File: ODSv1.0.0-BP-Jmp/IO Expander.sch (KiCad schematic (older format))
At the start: 15 parts, among them J20 Conn_02x10_Odd_Even, J21 Conn_02x10_Odd_Even, J22 Conn_02x10_Odd_Even, U3 MAX7317, U4 DACx0508xRTE, U5 AD7689xCP

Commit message: Fix incorrect pin type in the AD7689xCP symbol from KiCad
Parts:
- U5: symbol Analog_ADC:AD7689xCP -> Octopi:AD7689xCP
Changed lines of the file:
@@
 $EndComp
 $Comp
-L Analog_ADC:AD7689xCP U5
+L Octopi:AD7689xCP U5
 U 1 1 602154C4
 P 8000 3500

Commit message: Define a no-IC variant of BP-Jmp
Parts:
- U3, U4, U5: Config -NoExpansion -> -NoExpansion, -NoIC
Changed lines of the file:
@@
 F 7 "SMD" H 2500 1750 50  0001 C CNN "Type"
 F 8 "MAX7317AEE+TCT-ND" H 2500 1750 50  0001 C CNN "Digikey ID"
-F 9 "-NoExpansion" H 2500 1750 50  0001 C CNN "Config"
+F 9 "-NoExpansion, -NoIC" H 2500 1750 50  0001 C CNN "Config"
 	1    2500 1750
 	1    0    0    -1
@@
 F 2 "Package_DFN_QFN:WQFN-16-1EP_3x3mm_P0.5mm_EP1.6x1.6mm_ThermalVias" H 2500 3000 50  0001 C CNN
 F 3 "https://www.ti.com/lit/ds/symlink/dac60508.pdf" H 2500 3550 50  0001 C CNN
-F 4 "-NoExpansion" H 2500 3500 50  0001 C CNN "Config"
+F 4 "-NoExpansion, -NoIC" H 2500 3500 50  0001 C CNN "Config"
 F 5 "296-51047-1-ND" H 2500 3500 50  0001 C CNN "Digikey ID"
 F 6 "DAC80508ZRTER" H 2500 3500 50  0001 C CNN "MPN"
@@
 F 2 "Package_CSP:LFCSP-20-1EP_4x4mm_P0.5mm_EP2.5x2.5mm" H 8000 3500 50  0001 C CNN
 F 3 "https://www.analog.com/media/en/technical-documentation/data-sheets/AD7682_7689.pdf" H 8000 3500 50  0001 C CNN
-F 4 "-NoExpansion" H 8000 3500 50  0001 C CNN "Config"
+F 4 "-NoExpansion, -NoIC" H 8000 3500 50  0001 C CNN "Config"
 F 5 "AD7689BCPZRL7CT-ND" H 8000 3500 50  0001 C CNN "Digikey ID"
 F 6 "AD7689BCPZRL7" H 8000 3500 50  0001 C CNN "MPN"

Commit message: Fix problems with BP-Jmp variant configurations
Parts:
- C10, C11, C3, C4, C5, C6, C7, C8, C9: Config (none) -> -NoExpansion, -NoIC
- J20, J21, J22: Config -NoExpansion -> -NoExpansion, -NoIC
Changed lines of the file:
@@
 F 7 "SMD" H 750 1150 50  0001 C CNN "Type"
 F 8 "478-1235-1-ND" H 750 1150 50  0001 C CNN "Digikey ID"
+F 9 "-NoExpansion, -NoIC" H 750 1150 50  0001 C CNN "Config"
 	1    750  1150
 	1    0    0    -1
@@
 F 2 "Connector_PinHeader_2.54mm:PinHeader_2x10_P2.54mm_Vertical_SMD" H 3950 1700 50  0001 C CNN
 F 3 "http://suddendocs.samtec.com/catalog_english/tsm.pdf" H 3950 1700 50  0001 C CNN
-F 4 "-NoExpansion" H 3950 1700 50  0001 C CNN "Config"
+F 4 "-NoExpansion, -NoIC" H 3950 1700 50  0001 C CNN "Config"
 F 5 "SAM8990-ND" H 3950 1700 50  0001 C CNN "Digikey ID"
 F 6 "TSM-110-01-T-DV" H 3950 1700 50  0001 C CNN "MPN"
@@
 F 2 "Connector_PinHeader_2.54mm:PinHeader_2x10_P2.54mm_Vertical_SMD" H 4050 3400 50  0001 C CNN
 F 3 "http://suddendocs.samtec.com/catalog_english/tsm.pdf" H 4050 3400 50  0001 C CNN
-F 4 "-NoExpansion" H 4050 3400 50  0001 C CNN "Config"
+F 4 "-NoExpansion, -NoIC" H 4050 3400 50  0001 C CNN "Config"
 F 5 "SAM8990-ND" H 4050 3400 50  0001 C CNN "Digikey ID"
 F 6 "TSM-110-01-T-DV" H 4050 3400 50  0001 C CNN "MPN"
@@
 F 7 "SMD" H 750 3050 50  0001 C CNN "Type"
 F 8 "478-7018-1-ND" H 750 3050 50  0001 C CNN "Digikey ID"
+F 9 "-NoExpansion, -NoIC" H 750 3050 50  0001 C CNN "Config"
 	1    750  3050
 	1    0    0    -1
@@
 F 7 "SMD" H 750 3900 50  0001 C CNN "Type"
 F 8 "478-7018-1-ND" H 750 3900 50  0001 C CNN "Digikey ID"
+F 9 "-NoExpansion, -NoIC" H 750 3900 50  0001 C CNN "Config"
 	1    750  3900
 	1    0    0    -1
@@
 F 7 "SMD" H 1200 3050 50  0001 C CNN "Type"
 F 8 "478-10578-1-ND" H 1200 3050 50  0001 C CNN "Digikey ID"
+F 9 "-NoExpansion, -NoIC" H 1200 3050 50  0001 C CNN "Config"
 	1    1200 3050
 	1    0    0    -1
@@
 F 7 "SMD" H 1200 3900 50  0001 C CNN "Type"
 F 8 "478-7018-1-ND" H 1200 3900 50  0001 C CNN "Digikey ID"
+F 9 "-NoExpansion, -NoIC" H 1200 3900 50  0001 C CNN "Config"
 	1    1200 3900
 	1    0    0    -1
@@
 F 7 "SMD" H 6000 3150 50  0001 C CNN "Type"
 F 8 "478-7018-1-ND" H 6000 3150 50  0001 C CNN "Digikey ID"
+F 9 "-NoExpansion, -NoIC" H 6000 3150 50  0001 C CNN "Config"
 	1    6000 3150
 	-1   0    0    -1
@@
 F 2 "Connector_PinHeader_2.54mm:PinHeader_2x10_P2.54mm_Vertical_SMD" H 9300 3400 50  0001 C CNN
 F 3 "http://suddendocs.samtec.com/catalog_english/tsm.pdf" H 9300 3400 50  0001 C CNN
-F 4 "-NoExpansion" H 9300 3400 50  0001 C CNN "Config"
+F 4 "-NoExpansion, -NoIC" H 9300 3400 50  0001 C CNN "Config"
 F 5 "SAM8990-ND" H 9300 3400 50  0001 C CNN "Digikey ID"
 F 6 "TSM-110-01-T-DV" H 9300 3400 50  0001 C CNN "MPN"
@@
 F 7 "SMD" H 6500 3950 50  0001 C CNN "Type"
 F 8 "478-10578-1-ND" H 6500 3950 50  0001 C CNN "Digikey ID"
+F 9 "-NoExpansion, -NoIC" H 6500 3950 50  0001 C CNN "Config"
 	1    6500 3950
 	-1   0    0    -1
@@
 F 7 "SMD" H 6500 3150 50  0001 C CNN "Type"
 F 8 "478-7018-1-ND" H 6500 3150 50  0001 C CNN "Digikey ID"
+F 9 "-NoExpansion, -NoIC" H 6500 3150 50  0001 C CNN "Config"
 	1    6500 3150
 	-1   0    0    -1
@@
 F 7 "SMD" H 6000 3950 50  0001 C CNN "Type"
 F 8 "478-7018-1-ND" H 6000 3950 50  0001 C CNN "Digikey ID"
+F 9 "-NoExpansion, -NoIC" H 6000 3950 50  0001 C CNN "Config"
 	1    6000 3950
 	-1   0    0    -1

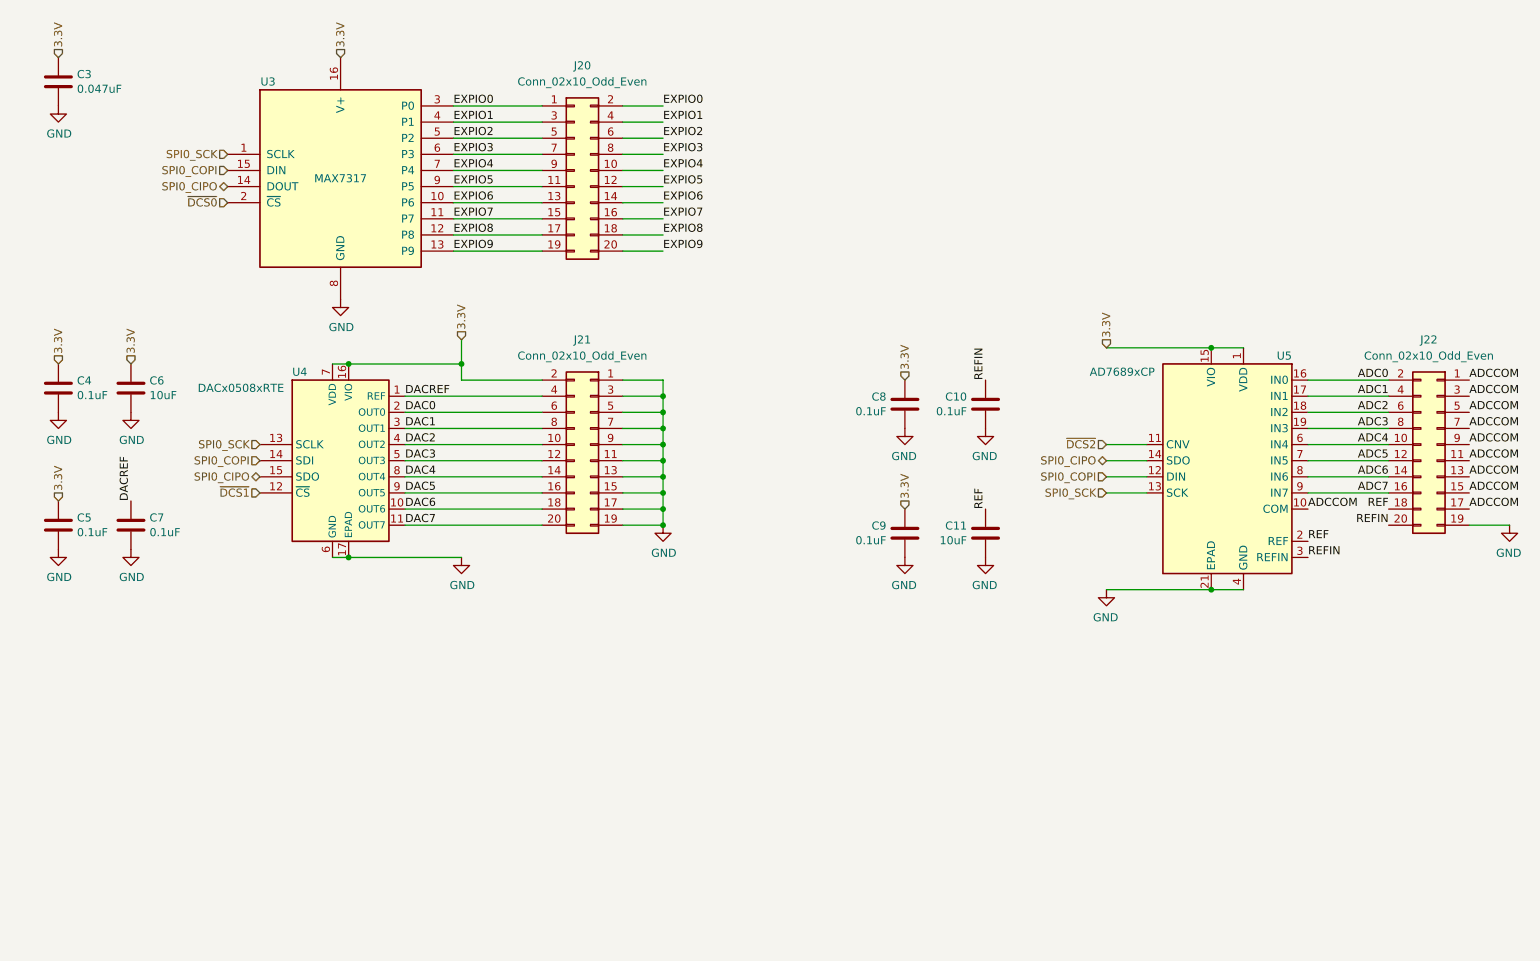
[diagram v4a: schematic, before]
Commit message: Fix implementation of SPI CS multiplexing system (#22)
* Disconnect PP-T41's MAX7317's DOUT, since it's not needed anyways (#16)

* Disconnect BT & BP-Jmp backbone MAX7317 DOUT (#16); make DOUT output pin

* Replace DAC with a second MAX7317 expander with pullup resistors

* Insert 3-state buffers between MAX7317 DOUTs and CIPO in BP-Jmp (#16)

* Update symbol fields for I/O expansion components in BP-Jmp

* Consolidate free space by moving the AD7689 chip

* Add pull-ups on demuxed DCS (#17), move pull-ups to bottom of BP-Jmp

* Insert 3-state buffers between all MAX7317 DOUTs and CIPO (#16)

* Add bypass caps to the 3-state buffers for BP-Jmp's I/O expanders

* Fix title block for SPI DCS Selector sheet in BP-Jmp

* Use 2k pullups instead of 20k pullups on BP-Jmp

* Add 2k pullups on demuxed DSCS pins in PP-T41

* Define a NoPufferfish BOM variant of PP-T41

* Adjust the 12V copper fills on PP-T41

* Add 2k pullups within the DSCS selector in PP-T41 (#17)

* Add more information to READMEs

* Add 2k pullups within DCS selectors (#17), bump BP-Jmp to 0.2.0

* Fix errors in PR template for modified boards

* Move usage on I/O peripherals into a subsection in BP-Jmp's README.md

* Update KiCad preview & mechanical renders of all boards

* Improve & consolidate pull request templates

* Update raytrace renders of the entire stack

* Add missing definition for NoPufferfish variant for PP-T41

* Add link to CADLab project for this repo

* Remove the message annoyingly added by CADLab to top of README.md
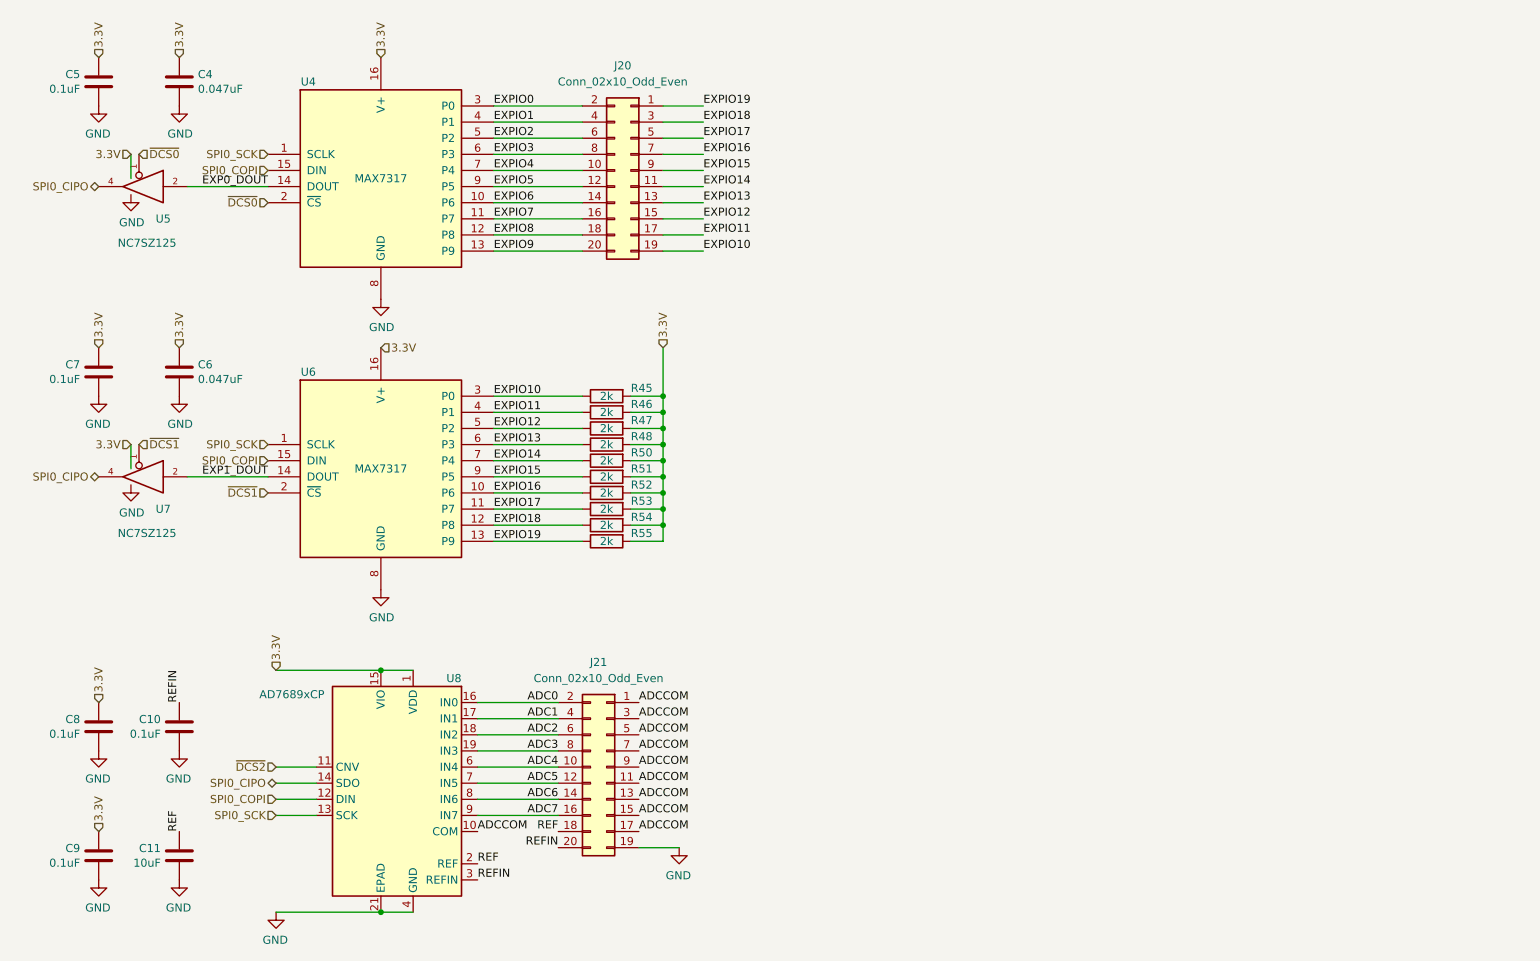
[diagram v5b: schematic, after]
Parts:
- removed C3: 0.047uF, Capacitor_SMD:C_0603_1608Metric, symbol Device:C
- removed J21: Conn_02x10_Odd_Even, Connector_PinHeader_2.54mm:PinHeader_2x10_P2.54mm_Vertical_SMD, symbol Connector_Generic:Conn_02x10_Odd_Even
- removed U4: DACx0508xRTE, Package_DFN_QFN:WQFN-16-1EP_3x3mm_P0.5mm_EP1.6x1.6mm_ThermalVias, symbol Octopi:DACx0508xRTE
- added R45, R46, R47, R48, R50, R51, R52, R53, R54, R55: 2k, Resistor_SMD:R_0603_1608Metric, symbol Device:R
- added U5, U7: NC7SZ125, Package_TO_SOT_SMD:SOT-353_SC-70-5, symbol Octopi:NC7SZ125
- added U6: MAX7317, Package_SO:QSOP-16_3.9x4.9mm_P0.635mm, symbol Octopi:MAX7317
- C4: value 0.1uF -> 0.047uF; Digikey ID 478-7018-1-ND -> 478-1235-1-ND; MPN 06033C104KAT4A -> 06033C473KAT2A; Ordering URL https://www.digikey.com/en/products/detail/avx-corporation/06033C104KAT4A/3247517 -> https://www.digikey.com/en/products/detail/avx-corporation/06033C473KAT2A/563345
- C6: value 10uF -> 0.047uF; footprint Capacitor_SMD:C_0805_2012Metric -> Capacitor_SMD:C_0603_1608Metric; Digikey ID 478-10578-1-ND -> 478-1235-1-ND; MPN 0805ZC106KAT2A -> 06033C473KAT2A; Ordering URL https://www.digikey.com/en/products/detail/avx-corporation/0805ZC106KAT2A/3081418 -> https://www.digikey.com/en/products/detail/avx-corporation/06033C473KAT2A/563345
- renumbered J22 to J21, U3 to U4, U5 to U8
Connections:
- net DACREF is gone; now on net VCC: C7.1
- net EXPIO0: no longer J20.1 (Pin_1)
- net EXPIO1: no longer J20.3 (Pin_3)
- net EXPIO2: no longer J20.5 (Pin_5)
- net EXPIO3: no longer J20.7 (Pin_7)
- net EXPIO4: no longer J20.9 (Pin_9)
- net EXPIO5: no longer J20.11 (Pin_11)
- net EXPIO6: no longer J20.13 (Pin_13)
- net EXPIO7: no longer J20.15 (Pin_15)
- net EXPIO8: no longer J20.17 (Pin_17)
- net EXPIO9: no longer J20.19 (Pin_19)
- net GND: now also U5.3 (GND), U6.8 (GND), U7.3 (GND)
- net SPI0_CIPO: now also U5.4, U7.4; no longer U4.14 (DOUT)
- net SPI0_COPI: now also U6.15 (DIN)
- net SPI0_SCK: now also U6.1 (SCLK)
- net ~DCS0~: now also U5.1
- net ~DCS1~: now also U6.2 (~CS~), U7.1
- net 3.3V renamed VCC
- net VCC: now also R45.2, R46.2, R47.2, R48.2, R50.2, R51.2, R52.2, R53.2, R54.2, R55.2, U5.5 (VCC), U6.16 (V+), U7.5 (VCC)
- new net EXP0_DOUT: U4.14 (DOUT), U5.2
- new net EXP1_DOUT: U6.14 (DOUT), U7.2
- new net EXPIO10: J20.19 (Pin_19), R45.1, U6.3 (P0)
- new net EXPIO11: J20.17 (Pin_17), R46.1, U6.4 (P1)
- new net EXPIO12: J20.15 (Pin_15), R47.1, U6.5 (P2)
- new net EXPIO13: J20.13 (Pin_13), R48.1, U6.6 (P3)
- new net EXPIO14: J20.11 (Pin_11), R50.1, U6.7 (P4)
- new net EXPIO15: J20.9 (Pin_9), R51.1, U6.9 (P5)
- new net EXPIO16: J20.7 (Pin_7), R52.1, U6.10 (P6)
- new net EXPIO17: J20.5 (Pin_5), R53.1, U6.11 (P7)
- new net EXPIO18: J20.3 (Pin_3), R54.1, U6.12 (P8)
- new net EXPIO19: J20.1 (Pin_1), R55.1, U6.13 (P9)
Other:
- moved on the sheet: C10, C11, C8, C9, J20, J21, U4, U8
